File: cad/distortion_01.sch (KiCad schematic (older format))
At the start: 89 parts, among them CON101 Ext_PSU, J101 JACK_IN, J102 JACK_OUT, P101 Battery_conn, P102 BYPASS_SWITCH, Q101 BS170, Q102 BS170, Q103 DTC114Y, SW101 OCTAVE_PRE_POST_SWITCH, SW102 HALF-FULLWAVE_SWITCH, U101 TL072, U102 4013, U103 TL071, U104 TL072, U105 4066, U106 TL074, U107 TL071

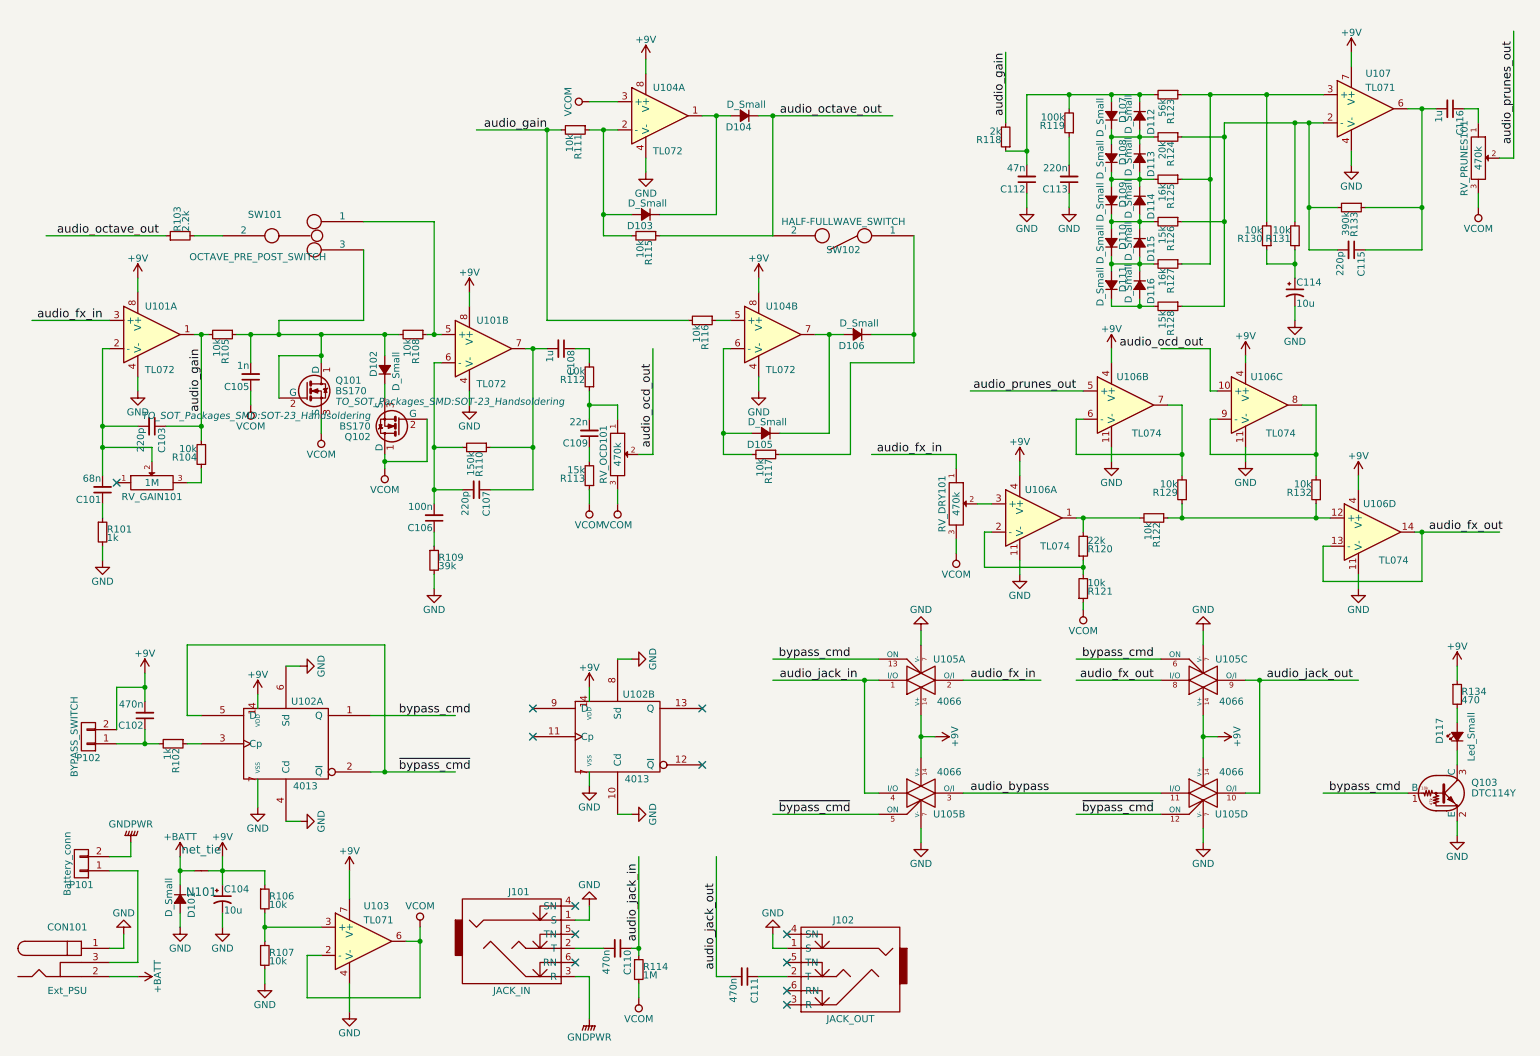
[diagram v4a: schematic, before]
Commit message: Placement started with 1590B cutout. Too small, 1590BB required.
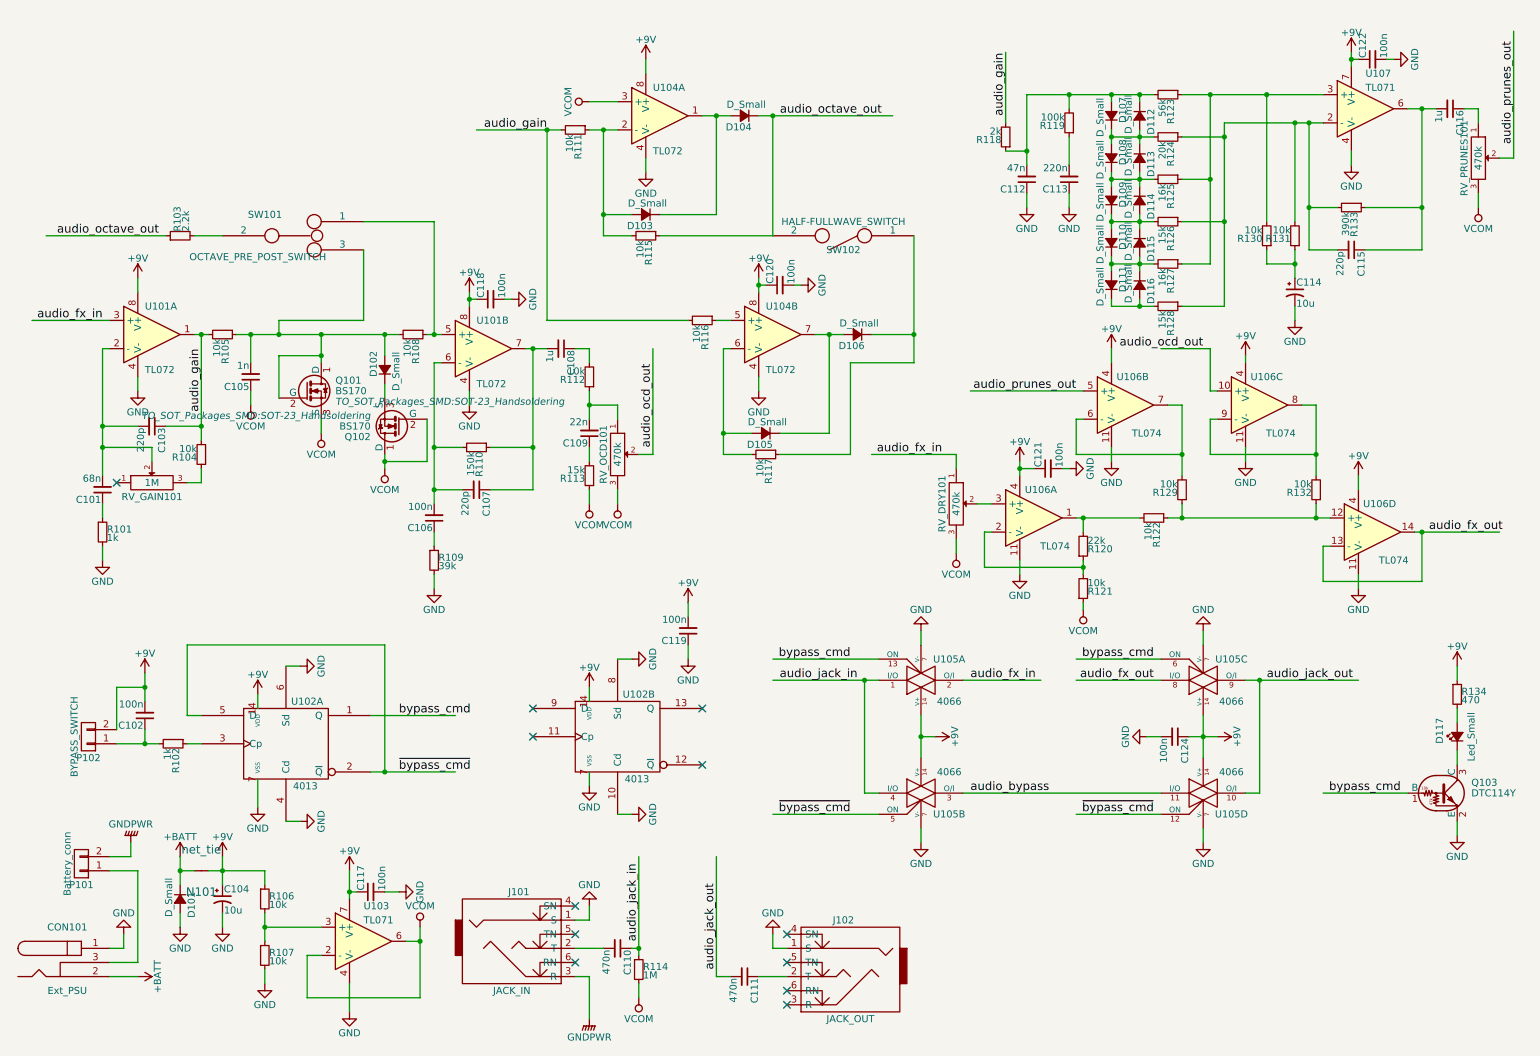
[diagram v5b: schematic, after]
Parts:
- added C117, C118, C119, C120, C121, C122, C124: 100n, Capacitors_SMD:C_0603_HandSoldering, symbol C_Small
- C102: value 470n -> 100n; footprint Capacitors_SMD:C_0805_HandSoldering -> Capacitors_SMD:C_0603_HandSoldering
- RV_DRY101, RV_GAIN101, RV_OCD101, RV_PRUNES101: footprint flax_lib:alpha_rv141F -> flax_lib:ALPHA_RV09
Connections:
- wire segments 267 -> 280

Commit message: Changed edge cuts to 1590BB. Made pre-placement.
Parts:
- RV_DRY101, RV_GAIN101, RV_OCD101, RV_PRUNES101: footprint flax_lib:ALPHA_RV09 -> flax_lib:alpha_rv141F
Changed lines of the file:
@@
 F 0 "RV_GAIN101" H 1500 3650 50  0000 C CNN
 F 1 "1M" H 1500 3750 50  0000 C CNN
-F 2 "flax_lib:ALPHA_RV09" H 1500 3750 50  0001 C CNN
+F 2 "flax_lib:alpha_rv141F" H 1500 3750 50  0001 C CNN
 F 3 "" H 1500 3750 50  0000 C CNN
 	1    1500 3750
@@
 F 0 "RV_OCD101" H 4800 3450 50  0000 C CNN
 F 1 "470k" H 4800 3550 50  0000 C CNN
-F 2 "flax_lib:ALPHA_RV09" H 4800 3550 50  0001 C CNN
+F 2 "flax_lib:alpha_rv141F" H 4800 3550 50  0001 C CNN
 F 3 "" H 4800 3550 50  0000 C CNN
 	1    4800 3550
@@
 F 0 "RV_PRUNES101" H 10900 1350 50  0000 C CNN
 F 1 "470k" H 10900 1450 50  0000 C CNN
-F 2 "flax_lib:ALPHA_RV09" H 10900 1450 50  0001 C CNN
+F 2 "flax_lib:alpha_rv141F" H 10900 1450 50  0001 C CNN
 F 3 "" H 10900 1450 50  0000 C CNN
 	1    10900 1450
@@
 F 0 "RV_DRY101" H 7200 3800 50  0000 C CNN
 F 1 "470k" H 7200 3900 50  0000 C CNN
-F 2 "flax_lib:ALPHA_RV09" H 7200 3900 50  0001 C CNN
+F 2 "flax_lib:alpha_rv141F" H 7200 3900 50  0001 C CNN
 F 3 "" H 7200 3900 50  0000 C CNN
 	1    7200 3900

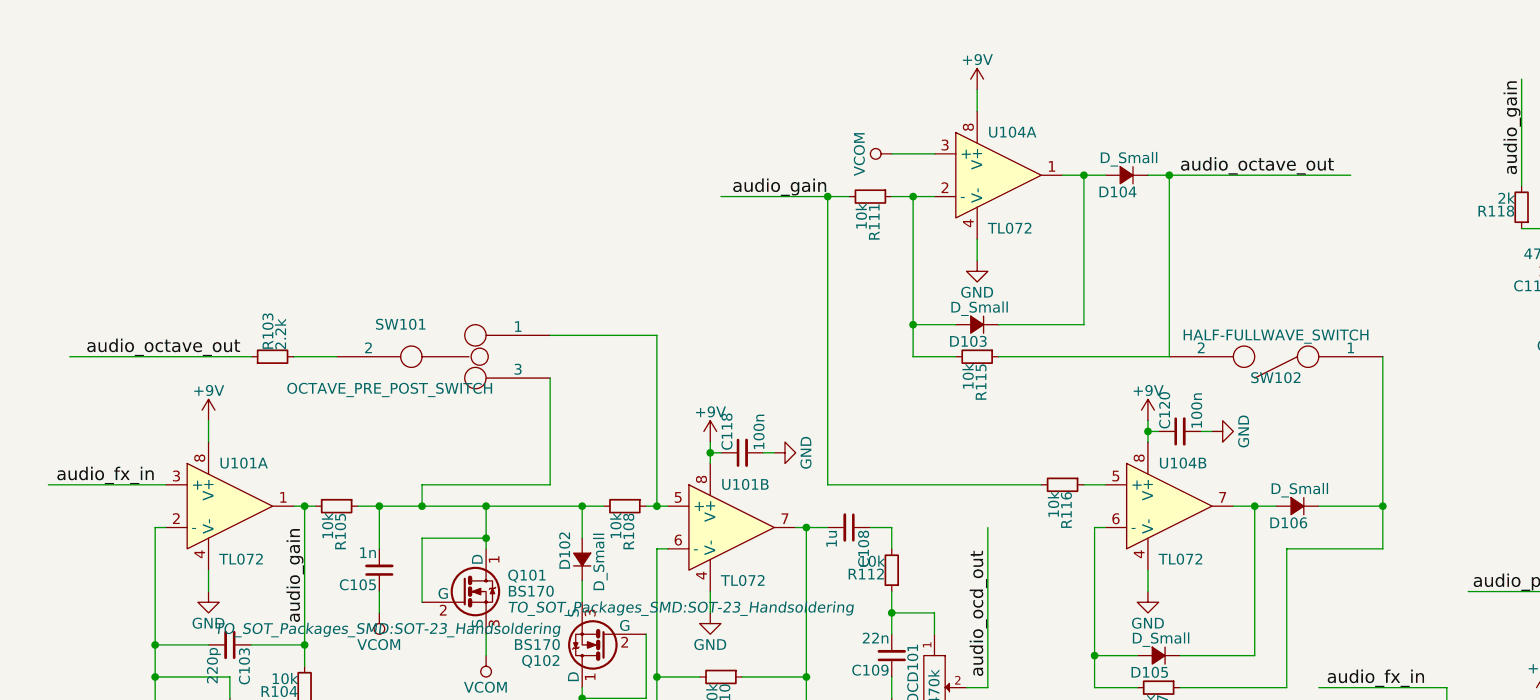
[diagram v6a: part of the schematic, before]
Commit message: Finished layout.
Added switch board.
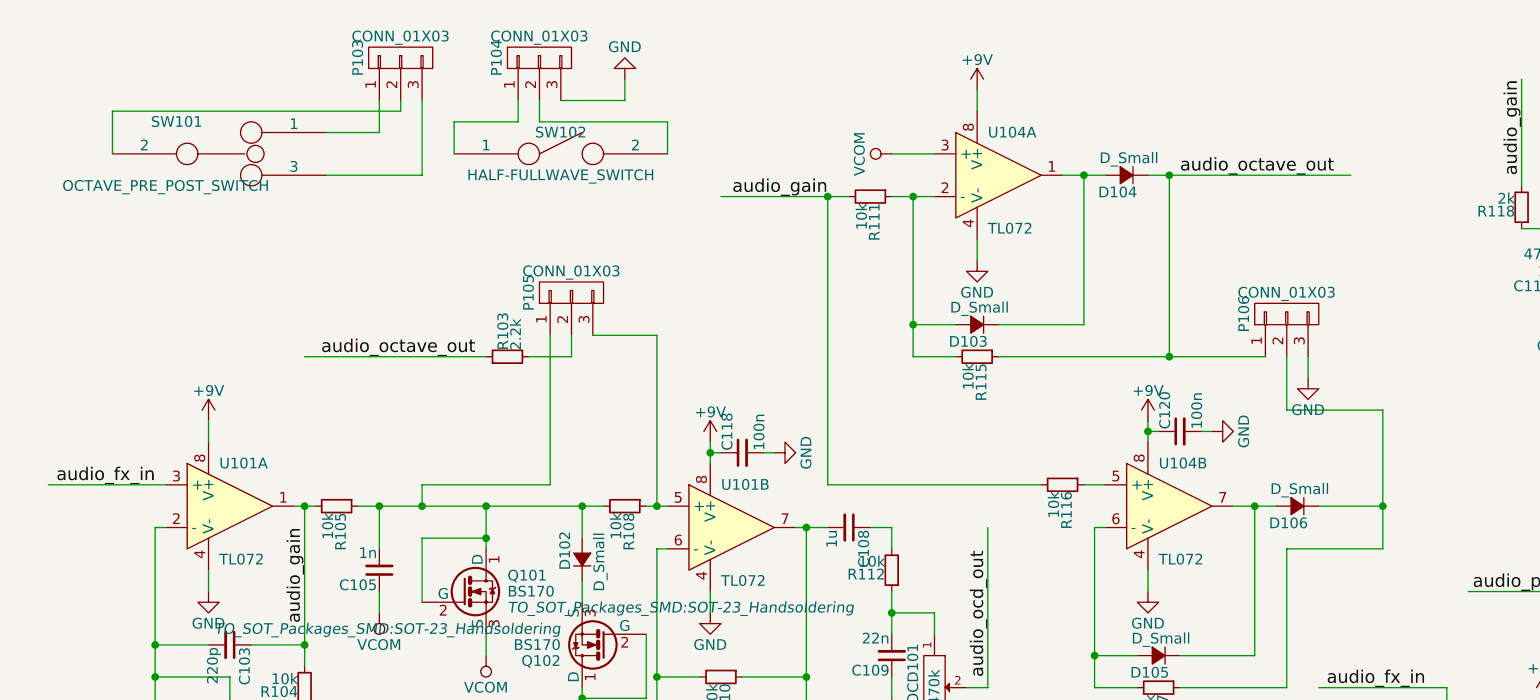
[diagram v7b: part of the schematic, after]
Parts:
- added P103, P104, P105, P106: CONN_01X03, Pin_Headers:Pin_Header_Straight_1x03_Pitch2.54mm, symbol CONN_01X03
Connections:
- wire segments 280 -> 299
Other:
- moved on the sheet: R103, SW101, SW102
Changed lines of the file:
@@
 L R_Small R103
 U 1 1 589F9DEF
-P 1700 2000
-F 0 "R103" H 1730 2020 50  0000 L CNN
-F 1 "2.2k" H 1730 1960 50  0000 L CNN
-F 2 "Resistors_SMD:R_0603_HandSoldering" H 1700 2000 50  0001 C CNN
-F 3 "" H 1700 2000 50  0000 C CNN
-	1    1700 2000
+P 2800 2000
+F 0 "R103" H 2830 2020 50  0000 L CNN
+F 1 "2.2k" H 2830 1960 50  0000 L CNN
+F 2 "Resistors_SMD:R_0603_HandSoldering" H 2800 2000 50  0001 C CNN
+F 3 "" H 2800 2000 50  0000 C CNN
+	1    2800 2000
 	0    -1   -1   0
 $EndComp
@@
 Text Label 4300 1250 2    60   ~ 0
 audio_gain
-Text Label 1550 2000 2    60   ~ 0
+Text Label 2650 2000 2    60   ~ 0
 audio_octave_out
 Text Label 5950 1150 0    60   ~ 0
@@
 L SWITCH_INV_MSM SW101
 U 1 1 589FE151
-P 2500 2000
-F 0 "SW101" H 2301 2150 50  0000 C CNN
-F 1 "OCTAVE_PRE_POST_SWITCH" H 2250 1850 50  0000 C CNN
-F 2 "flax_lib:SW_SPDT_through_hole" H 2500 2000 50  0001 C CNN
-F 3 "" H 2500 2000 50  0000 C CNN
-	1    2500 2000
+P 1450 1050
+F 0 "SW101" H 1251 1200 50  0000 C CNN
+F 1 "OCTAVE_PRE_POST_SWITCH" H 1200 900 50  0000 C CNN
+F 2 "flax_lib:SW_SPDT_through_hole" H 1450 1050 50  0001 C CNN
+F 3 "" H 1450 1050 50  0000 C CNN
+	1    1450 1050
 	1    0    0    -1
 $EndComp
@@
 Connection ~ 5500 1150
 Wire Wire Line
-	5100 2000 5900 2000
-Wire Wire Line
 	5900 2000 5900 1150
 Connection ~ 5900 1150
@@
 	5800 1150 6750 1150
 Wire Wire Line
-	1600 2000 750  2000
+	2700 2000 1850 2000
 Connection ~ 3500 2700
 Wire Wire Line
@@
 	3500 1900 3500 2700
 Wire Wire Line
-	1800 2000 2000 2000
-Wire Wire Line
-	3000 2100 3000 2600
+	3000 1900 3000 2600
 Wire Wire Line
 	3000 2600 2400 2600
-Wire Wire Line
-	3000 1900 3500 1900
 $Comp
 L TL072 U104
@@
 L SPST SW102
 U 1 1 58A0DBD6
-P 6400 2000
-F 0 "SW102" H 6400 2100 50  0000 C CNN
-F 1 "HALF-FULLWAVE_SWITCH" H 6400 1900 50  0000 C CNN
-F 2 "flax_lib:SW_SPDT_through_hole" H 6400 2000 50  0001 C CNN
-F 3 "" H 6400 2000 50  0000 C CNN
-	1    6400 2000
-	-1   0    0    1
-$EndComp
-Wire Wire Line
-	6900 2000 6900 2900
+P 3050 1050
+F 0 "SW102" H 3050 1150 50  0000 C CNN
+F 1 "HALF-FULLWAVE_SWITCH" H 3050 950 50  0000 C CNN
+F 2 "flax_lib:SW_SPDT_through_hole" H 3050 1050 50  0001 C CNN
+F 3 "" H 3050 1050 50  0000 C CNN
+	1    3050 1050
+	1    0    0    -1
+$EndComp
 Wire Wire Line
 	6900 2700 6600 2700
@@
 Wire Wire Line
 	8550 5550 8650 5550
+$Comp
+L CONN_01X03 P105
+U 1 1 58B1CACE
+P 3100 1700
+F 0 "P105" H 3100 1900 50  0000 C CNN
+F 1 "CONN_01X03" V 3200 1700 50  0000 C CNN
+F 2 "Pin_Headers:Pin_Header_Straight_1x03_Pitch2.54mm" H 3100 1700 50  0001 C CNN
+F 3 "" H 3100 1700 50  0000 C CNN
+	1    3100 1700
+	0    -1   -1   0
+$EndComp
+$Comp
+L CONN_01X03 P103
+U 1 1 58B1CC4D
+P 2300 600
+F 0 "P103" H 2300 800 50  0000 C CNN
+F 1 "CONN_01X03" V 2400 600 50  0000 C CNN
+F 2 "Pin_Headers:Pin_Header_Straight_1x03_Pitch2.54mm" H 2300 600 50  0001 C CNN
+F 3 "" H 2300 600 50  0000 C CNN
+	1    2300 600
+	0    -1   -1   0
+$EndComp
+Wire Wire Line
+	2200 800  2200 950
+Wire Wire Line
+	2200 950  1950 950
+Wire Wire Line
+	2400 800  2400 1150
+Wire Wire Line
+	2400 1150 1950 1150
+Wire Wire Line
+	950  1050 950  850
+Wire Wire Line
+	950  850  2300 850
+Wire Wire Line
+	2300 850  2300 800
+Connection ~ 5900 2000
+$Comp
+L CONN_01X03 P106
+U 1 1 58B21900
+P 6450 1800
+F 0 "P106" H 6450 2000 50  0000 C CNN
+F 1 "CONN_01X03" V 6550 1800 50  0000 C CNN
+F 2 "Pin_Headers:Pin_Header_Straight_1x03_Pitch2.54mm" H 6450 1800 50  0001 C CNN
+F 3 "" H 6450 1800 50  0000 C CNN
+	1    6450 1800
+	0    -1   -1   0
+$EndComp
+Wire Wire Line
+	6350 2000 5100 2000
+$Comp
+L CONN_01X03 P104
+U 1 1 58B231BF
+P 2950 600
+F 0 "P104" H 2950 800 50  0000 C CNN
+F 1 "CONN_01X03" V 3050 600 50  0000 C CNN
+F 2 "Pin_Headers:Pin_Header_Straight_1x03_Pitch2.54mm" H 2950 600 50  0001 C CNN
+F 3 "" H 2950 600 50  0000 C CNN
+	1    2950 600
+	0    -1   -1   0
+$EndComp
+Wire Wire Line
+	2850 800  2850 900
+Wire Wire Line
+	2850 900  2550 900
+Wire Wire Line
+	2550 900  2550 1050
+Wire Wire Line
+	3550 1050 3550 900
+Wire Wire Line
+	3550 900  2950 900
+Wire Wire Line
+	2950 900  2950 800
+Wire Wire Line
+	6450 2000 6450 2250
+Wire Wire Line
+	6900 2900 6900 2250
+Wire Wire Line
+	6900 2250 6450 2250
+Wire Wire Line
+	3100 2000 3100 1900
+Wire Wire Line
+	3500 1900 3200 1900
+Wire Wire Line
+	3100 2000 2900 2000
+$Comp
+L GND #PWR?
+U 1 1 58B2C97E
+P 6550 2100
+F 0 "#PWR?" H 6550 1850 50  0001 C CNN
+F 1 "GND" H 6550 1950 50  0000 C CNN
+F 2 "" H 6550 2100 50  0000 C CNN
+F 3 "" H 6550 2100 50  0000 C CNN
+	1    6550 2100
+	1    0    0    -1
+$EndComp
+Wire Wire Line
+	6550 2100 6550 2000
+$Comp
+L GND #PWR?
+U 1 1 58B2CCB0
+P 3350 700
+F 0 "#PWR?" H 3350 450 50  0001 C CNN
+F 1 "GND" H 3350 550 50  0000 C CNN
+F 2 "" H 3350 700 50  0000 C CNN
+F 3 "" H 3350 700 50  0000 C CNN
+	1    3350 700
+	-1   0    0    1
+$EndComp
+Wire Wire Line
+	3050 800  3350 800
+Wire Wire Line
+	3350 800  3350 700
 $EndSCHEMATC

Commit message: Minor corrections.
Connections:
- wire segments 299 -> 300
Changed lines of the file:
@@
 	3100 2000 2900 2000
 $Comp
-L GND #PWR?
+L GND #PWR073
 U 1 1 58B2C97E
 P 6550 2100
-F 0 "#PWR?" H 6550 1850 50  0001 C CNN
+F 0 "#PWR073" H 6550 1850 50  0001 C CNN
 F 1 "GND" H 6550 1950 50  0000 C CNN
 F 2 "" H 6550 2100 50  0000 C CNN
@@
 	6550 2100 6550 2000
 $Comp
-L GND #PWR?
+L GND #PWR074
 U 1 1 58B2CCB0
 P 3350 700
-F 0 "#PWR?" H 3350 450 50  0001 C CNN
+F 0 "#PWR074" H 3350 450 50  0001 C CNN
 F 1 "GND" H 3350 550 50  0000 C CNN
 F 2 "" H 3350 700 50  0000 C CNN
@@
 Wire Wire Line
 	3350 800  3350 700
+$Comp
+L PWR_FLAG #FLG075
+U 1 1 58B203AC
+P 1250 7350
+F 0 "#FLG075" H 1250 7445 50  0001 C CNN
+F 1 "PWR_FLAG" H 1250 7530 50  0000 C CNN
+F 2 "" H 1250 7350 50  0000 C CNN
+F 3 "" H 1250 7350 50  0000 C CNN
+	1    1250 7350
+	-1   0    0    1
+$EndComp
+Wire Wire Line
+	1250 7350 1250 7250
+Connection ~ 1250 7250
 $EndSCHEMATC
